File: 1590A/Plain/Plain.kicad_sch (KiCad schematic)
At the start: 17 parts, among them J101 Conn_01x04_Pin, J102 Barrel_Jack_Switch, J103 Conn_01x04_Pin, J104 AudioJack2_Ground, J105 AudioJack2_Ground, Q101 PMV250, Q102 BC847C

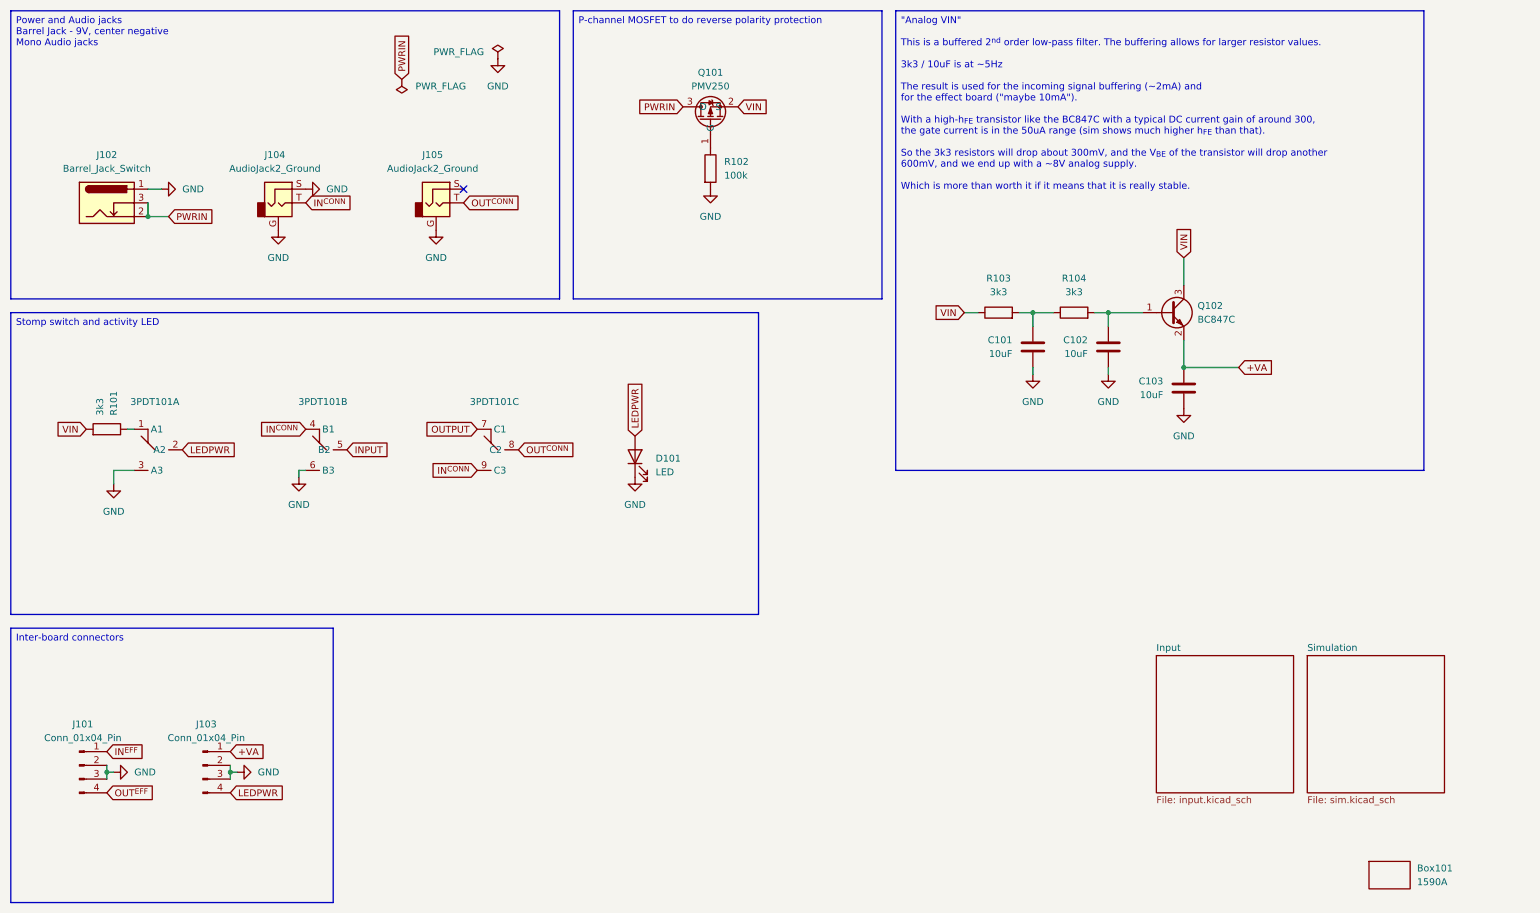
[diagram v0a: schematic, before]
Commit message: Update plain 1590A board
I had decided that the effect board didn't need the input to be
ground-biased, and that was very wrong, and made some of my old effect
boards not work.  So add the AC couple capacitor and resistor to ground.

Also do the same boring RC power smoothing with the voodoo ferrite for
the +VA line.  Let's keep it simple and realistic - the noise isn't some
60Hz ripple, it's all SMPS high-frequency stuff.

Signed-off-by: Linus Torvalds <torvalds@linux-foundation.org>
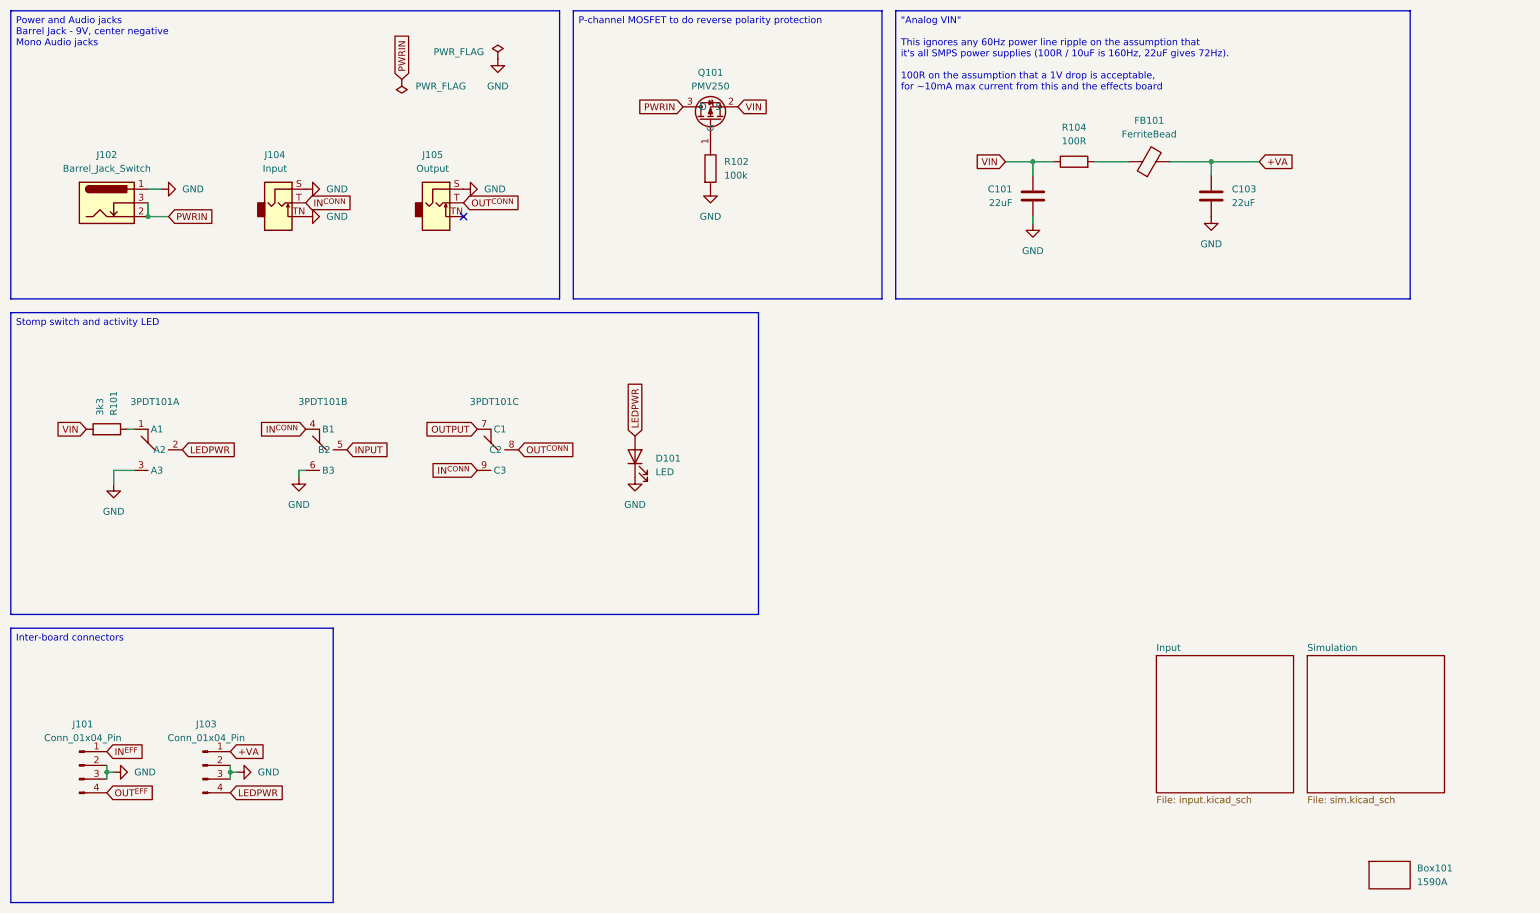
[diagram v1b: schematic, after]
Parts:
- removed C102: 10uF, Capacitor_SMD:C_1206_3216Metric, symbol Device:C
- removed Q102: BC847C, Package_TO_SOT_SMD:SOT-23, symbol Mylib:BC847C
- removed R103: 3k3, Resistor_SMD:R_0805_2012Metric, symbol Device:R
- added FB101: FerriteBead, Inductor_SMD:L_1206_3216Metric, symbol Device:FerriteBead
- C101, C103: value 10uF -> 22uF
- J104: value AudioJack2_Ground -> Input; symbol Connector_Audio:AudioJack2_Ground -> Connector_Audio:AudioJack2_SwitchT
- J105: value AudioJack2_Ground -> Output; symbol Connector_Audio:AudioJack2_Ground -> Connector_Audio:AudioJack2_SwitchT
- R104: value 3k3 -> 100R
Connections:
- net +VA: now also FB101.2
- net GND: now also J104.TN, J105.S; no longer J104.G, J105.G
- net VIN: now also C101.1, R104.1
- net at R104.2: now also FB101.1
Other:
- moved on the sheet: C101, C103, R104
